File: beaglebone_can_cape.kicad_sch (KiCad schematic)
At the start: 8 parts, among them J1 DCAN0, J2 DCAN1, P8 BeagleBone_Black_Header, P9 BeagleBone_Black_Header, U1 TCAN332, U2 TCAN332

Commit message: finished sch, adding footprints now
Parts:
- added JP1, JP2: Jumper_2_Open, Connector_PinHeader_2.54mm:PinHeader_1x02_P2.54mm_Vertical, symbol Jumper:Jumper_2_Open
- added R1, R2: 120, symbol Device:R_Small_US
- J1, J2: footprint (none) -> TerminalBlock_RND:TerminalBlock_RND_205-00232_1x02_P5.08mm_Horizontal
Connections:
- net at J1.1 (Pin_1), U1.6 (CANL): now also R1.2
- net at J1.2 (Pin_2), U1.7 (CANH): now also JP1.1 (A)
- net at J2.1 (Pin_1), U2.6 (CANL): now also R2.2
- net at J2.2 (Pin_2), U2.7 (CANH): now also JP2.1 (A)
- new net: JP1.2 (B), R1.1
- new net: JP2.2 (B), R2.1
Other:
- moved on the sheet: C1, C2, J1, J2, P8, P9, U1, U2

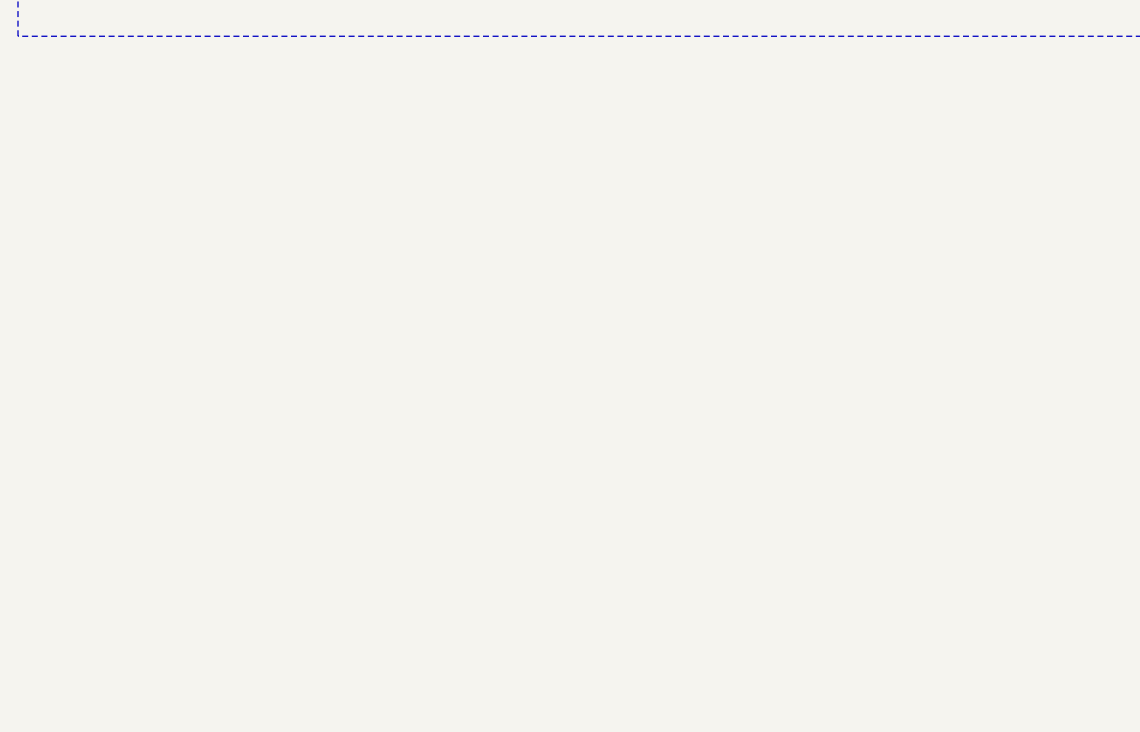
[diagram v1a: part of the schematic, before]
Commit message: Had to fork to commit (no write access to main)
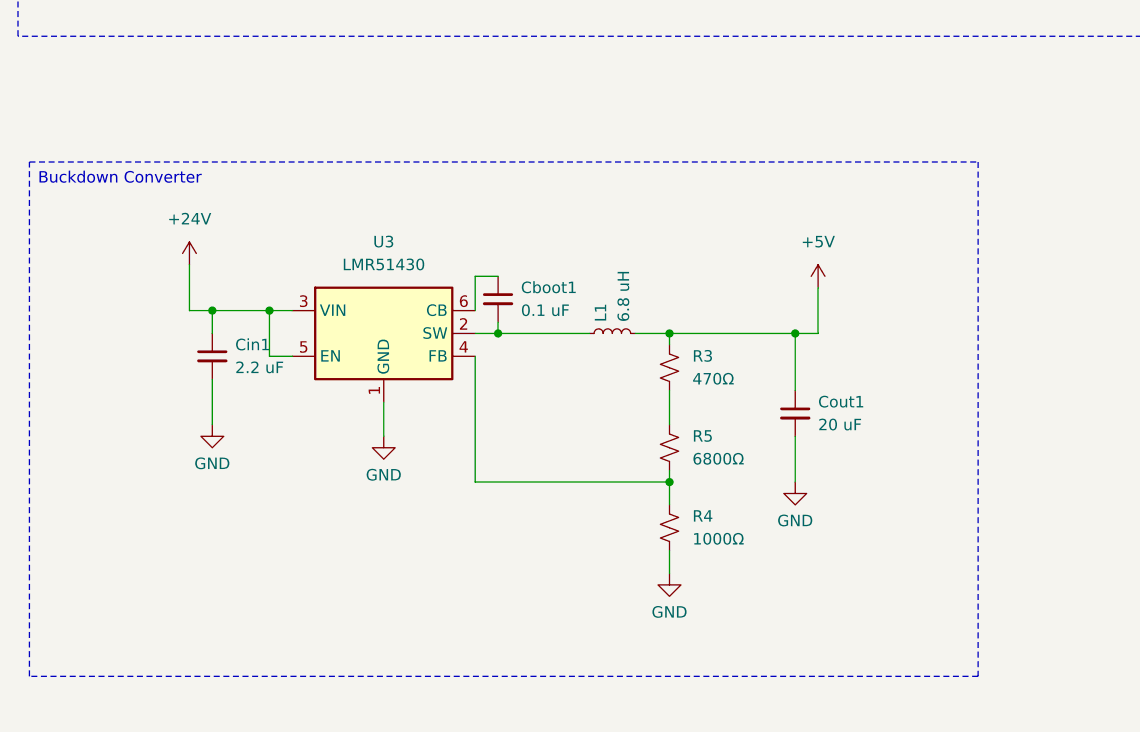
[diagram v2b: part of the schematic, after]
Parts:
- added Cboot1: 0.1 uF, Capacitor_THT:CP_Axial_L10.0mm_D4.5mm_P15.00mm_Horizontal, symbol Device:C_Small
- added Cin1: 2.2 uF, Capacitor_THT:CP_Axial_L10.0mm_D4.5mm_P15.00mm_Horizontal, symbol Device:C_Small
- added Cout1: 20 uF, Capacitor_THT:CP_Axial_L10.0mm_D4.5mm_P15.00mm_Horizontal, symbol Device:C_Small
- added L1: 6.8 uH, Inductor_THT:L_Axial_L5.0mm_D3.6mm_P10.00mm_Horizontal_Murata_BL01RN1A2A2, symbol Device:L_Small
- added R3: 470Ω, Resistor_THT:R_Axial_DIN0204_L3.6mm_D1.6mm_P1.90mm_Vertical, symbol Device:R_Small_US
- added R4: 1000Ω, Resistor_THT:R_Axial_DIN0204_L3.6mm_D1.6mm_P1.90mm_Vertical, symbol Device:R_Small_US
- added R5: 6800Ω, Resistor_THT:R_Axial_DIN0204_L3.6mm_D1.6mm_P1.90mm_Vertical, symbol Device:R_Small_US
- added U3: LMR51430, Package_TO_SOT_SMD:SOT-23-6, symbol Regulator_Switching:LMR51430
- R1, R2: footprint (none) -> Resistor_THT:R_Axial_DIN0204_L3.6mm_D1.6mm_P1.90mm_Vertical
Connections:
- net +5V: now also Cout1.1, L1.2, R3.1
- net GND: now also Cin1.2, Cout1.2, R4.2, U3.1 (GND)
- new net: Cboot1.2, L1.1, U3.2 (SW)
- new net: R4.1, R5.2, U3.4 (FB)
- new net: Cboot1.1, U3.6 (CB)
- new net: R3.2, R5.1
- new net +24V: Cin1.1, U3.3 (VIN), U3.5 (EN)
